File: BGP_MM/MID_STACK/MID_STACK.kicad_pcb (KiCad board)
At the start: 2 copper layers, 20 x 26 mm, 7 parts, among them P1 CONN_01X04, P2 CONN_01X09

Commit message: MM Finished board layouts
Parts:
- added J1: Conn_01x04_Male, Connectors_JST:JST_PH_B4B-PH-K_04x2.00mm_Straight, B.Cu at (152.0, 88.8)
- added J2: Conn_01x02_Male, Connectors_JST:JST_PH_B2B-PH-K_02x2.00mm_Straight, B.Cu at (148.0, 83.6)
- added J3: Conn_01x04_Male, Connectors_JST:JST_PH_B4B-PH-K_04x2.00mm_Straight, B.Cu at (152.0, 99.2)
- added J4: Conn_01x04_Male, Connectors_JST:JST_PH_B4B-PH-K_04x2.00mm_Straight, B.Cu at (152.0, 94.0)
- added P3: CONN_01X02, Terminal_Blocks:TerminalBlock_Pheonix_MPT-2.54mm_2pol, B.Cu at (144.8, 105.6)
- added P4: CONN_01X03, Terminal_Blocks:TerminalBlock_Pheonix_MPT-2.54mm_3pol, B.Cu at (153.1, 105.6)
- C1, C2: footprint Capacitor_THT:C_Rect_L7.2mm_W2.5mm_P5.00mm_FKS2_FKP2_MKS2_MKP2 -> Capacitor_THT:C_Rect_L4.6mm_W3.0mm_P2.50mm_MKS02_FKP02
- P1: value CONN_01X04 -> CONN_01X09; footprint Connectors_JST:JST_PH_B4B-PH-K_04x2.00mm_Straight -> LIBS:Potentiometer_Alpha_Tripple_Vertical_Dual_Shaft
- P2: value CONN_01X09 -> CONN_01X02; footprint LIBS:Potentiometer_Alpha_Tripple_Vertical_Dual_Shaft -> Terminal_Blocks:TerminalBlock_Pheonix_MPT-2.54mm_2pol
- R1: value 4.7k -> 200k
- R2: value 4.7k -> 10k
- R3: value 100k -> 10k
- moved C2 54.3 mm to (130.5, 103.6), turned to 0 degrees
- moved P1 50.1 mm to (132.2, 84.5), turned to 90 degrees
- moved R2 46.5 mm to (137.0, 99.5), turned to 0 degrees
- moved C1 36.5 mm to (130.6, 107.2), turned to 0 degrees
- moved R1 35.6 mm to (132.0, 99.5), turned to 180 degrees
- moved P2 34.2 mm to (139.1, 105.6), turned to 180 degrees
- moved R3 31.5 mm to (142.0, 99.5)
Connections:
- C2 pad 1: /F1_1 -> /MID_R
- P1 pad 1: /MID_I -> Net-(P1-Pad1)
- P1 pad 2: /F1_1 -> /F1_2
- P1 pad 3: /MID_O -> /MID_R
- P1 pad 4: /Vref -> Net-(P1-Pad4)
- P2 pad 1: Net-(P2-Pad1) -> /JZ_I
- P2 pad 2: /F1_2 -> Earth
- R1 pad 2: /F1_2 -> /MID_R
- R2 pad 1: /F2_2 -> Net-(C1-Pad2)
- R2 pad 2: /Vref -> /F1_2
- R3 pad 1: Net-(C1-Pad2) -> /F2_2
- R3 pad 2: /F1_1 -> /Vref
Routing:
- net /MID_R: track 0.00 -> 45.8 mm
- net /F1_1: track 36.3 -> 0.00 mm
- net /JZ_I: track 0.00 -> 18.0 mm
- net /MID_I: track 11.4 -> 26.6 mm
- net /SIG_O: track 0.00 -> 13.0 mm
- net /MM_BH: track 0.00 -> 12.1 mm
- net /MM_NH: track 0.00 -> 7.73 mm
- net /MM_BC: track 0.00 -> 6.63 mm
- net /F2_2: track 15.9 -> 12.0 mm
- net /F1_2: track 14.7 -> 17.5 mm
- net /VOL2: track 16.4 -> 14.9 mm
- net /MID_O: track 12.1 -> 13.3 mm
- net Net-(C1-Pad2): track 12.8 -> 11.7 mm
- added copper zone on B.Cu, net Earth
- removed copper zone on B.Cu, net (none)
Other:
- board size 20 x 26 mm -> 26 x 28 mm

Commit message: MM Tweaks
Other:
- board text added: "MM Sabre Mid Stack CBD Design"
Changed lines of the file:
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@@
     (links 24)
     (no_connects 0)
-    (area 128.924999 80.924999 155.075001 109.075001)
+    (area 127.485 78.666666 155.203001 111.03588)
     (thickness 1.6)
-    (drawings 8)
+    (drawings 9)
     (tracks 64)
     (zones 0)
@@
     )
   )
+  (gr_text "MM Sabre\nMid Stack\nCBD Design" (at 151.8 84) (layer F.SilkS)
+    (effects (font (size 0.6 0.6) (thickness 0.15)))
+  )
   (gr_line (start 129.3 108.7) (end 154.7 108.7) (layer Margin) (width 0.2))

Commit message: MM - Board changes
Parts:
- removed J2: Conn_01x02_Male, Connectors_JST:JST_PH_B2B-PH-K_02x2.00mm_Straight
- removed J3, J4: Conn_01x04_Male, Connectors_JST:JST_PH_B4B-PH-K_04x2.00mm_Straight
- removed P2, P3: CONN_01X02, Terminal_Blocks:TerminalBlock_Pheonix_MPT-2.54mm_2pol
- removed P4: CONN_01X03, Terminal_Blocks:TerminalBlock_Pheonix_MPT-2.54mm_3pol
- C1: footprint Capacitor_THT:C_Rect_L4.6mm_W3.0mm_P2.50mm_MKS02_FKP02 -> Capacitors_SMD:C_0805; moved to F.Cu
- C2: footprint Capacitor_THT:C_Rect_L4.6mm_W3.0mm_P2.50mm_MKS02_FKP02 -> Capacitors_SMD:C_1206; moved to F.Cu
- moved C1 8.98 mm to (137.1, 101.0), turned to 180 degrees
- moved J1 5.90 mm to (146.4, 90.7), turned to 90 degrees
- moved C2 3.00 mm to (132.0, 101.0)
- moved R1 1.50 mm to (132.0, 98.0)
- moved R2 1.50 mm to (137.0, 98.0)
- moved R3 1.50 mm to (142.0, 98.0)
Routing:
- net /JZ_I: track 18.0 -> 0.00 mm
- net /SIG_O: track 13.0 -> 0.00 mm
- net /MM_BH: track 12.1 -> 0.00 mm
- net /MID_R: track 45.8 -> 34.6 mm
- net /MM_NH: track 7.73 -> 0.00 mm
- net /MM_BC: track 6.63 -> 0.00 mm
- net Net-(C1-Pad2): track 11.7 -> 5.88 mm
- net /VOL2: track 14.9 -> 9.70 mm
- net /MID_O: track 13.3 -> 9.83 mm
- net /F1_2: track 17.5 -> 14.4 mm, vias 0 -> 1
- net /MID_I: track 26.6 -> 29.5 mm
- net /Vref: track 0.00 -> 1.00 mm, vias 0 -> 1
- added copper zone on B.Cu, net /Vref
- removed copper zone on B.Cu, net Earth
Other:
- board size 26 x 28 mm -> 19.5 x 21.5 mm

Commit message: tweaks
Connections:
- J1 pad 1: /Vref -> /MID_I
- J1 pad 2: /MID_O -> /MID_R
- J1 pad 3: /MID_R -> /MID_O
- J1 pad 4: /MID_I -> /Vref
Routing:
- net /MID_I: track 29.5 -> 20.1 mm
- net /MID_O: track 9.83 -> 11.3 mm
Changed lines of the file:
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@@
     )
     (pad 1 thru_hole rect (at 0 0 90) (size 1.2 1.7) (drill 0.75) (layers *.Cu *.Mask)
+      (net 4 /MID_I))
+    (pad 2 thru_hole oval (at 2 0 90) (size 1.2 1.7) (drill 0.75) (layers *.Cu *.Mask)
+      (net 10 /MID_R))
+    (pad 3 thru_hole oval (at 4 0 90) (size 1.2 1.7) (drill 0.75) (layers *.Cu *.Mask)
+      (net 5 /MID_O))
+    (pad 4 thru_hole oval (at 6 0 90) (size 1.2 1.7) (drill 0.75) (layers *.Cu *.Mask)
       (net 3 /Vref))
-    (pad 2 thru_hole oval (at 2 0 90) (size 1.2 1.7) (drill 0.75) (layers *.Cu *.Mask)
-      (net 5 /MID_O))
-    (pad 3 thru_hole oval (at 4 0 90) (size 1.2 1.7) (drill 0.75) (layers *.Cu *.Mask)
-      (net 10 /MID_R))
-    (pad 4 thru_hole oval (at 6 0 90) (size 1.2 1.7) (drill 0.75) (layers *.Cu *.Mask)
-      (net 4 /MID_I))
     (model ${KISYS3DMOD}/Connectors_JST.3dshapes/JST_PH_B4B-PH-K_04x2.00mm_Straight.wrl
       (at (xyz 0 0 0))
@@
   (segment (start 133.5 101) (end 134.5 101) (width 0.4) (layer F.Cu) (net 3))
   (via (at 134.5 101) (size 0.6) (drill 0.4) (layers F.Cu B.Cu) (net 3))
-  (segment (start 130.05 84) (end 130.05 92.3) (width 0.4) (layer B.Cu) (net 4))
-  (segment (start 130.05 92.3) (end 132.25 94.5) (width 0.4) (layer B.Cu) (net 4))
-  (segment (start 131.85 82.2) (end 130.05 84) (width 0.4) (layer B.Cu) (net 4))
-  (segment (start 142.7 82.2) (end 131.85 82.2) (width 0.4) (layer B.Cu) (net 4))
-  (segment (start 146.4 84.65) (end 145.15 84.65) (width 0.4) (layer B.Cu) (net 4))
-  (segment (start 145.15 84.65) (end 142.7 82.2) (width 0.4) (layer B.Cu) (net 4))
-  (segment (start 139.75 94.5) (end 139.75 93.2) (width 0.4) (layer B.Cu) (net 5))
-  (segment (start 139.75 93.2) (end 144.3 88.65) (width 0.4) (layer B.Cu) (net 5))
-  (segment (start 144.3 88.65) (end 146.4 88.65) (width 0.4) (layer B.Cu) (net 5))
+  (segment (start 141.45 98) (end 135.75 98) (width 0.4) (layer B.Cu) (net 4))
+  (segment (start 135.75 98) (end 132.25 94.5) (width 0.4) (layer B.Cu) (net 4))
+  (segment (start 146.4 93.05) (end 141.45 98) (width 0.4) (layer B.Cu) (net 4))
+  (segment (start 146.4 90.65) (end 146.4 93.05) (width 0.4) (layer B.Cu) (net 4))
+  (segment (start 146.4 86.65) (end 145.15 86.65) (width 0.4) (layer B.Cu) (net 5))
+  (segment (start 145.15 86.65) (end 142.85 88.95) (width 0.4) (layer B.Cu) (net 5))
+  (segment (start 142.85 88.95) (end 142.85 91.4) (width 0.4) (layer B.Cu) (net 5))
+  (segment (start 142.85 91.4) (end 139.75 94.5) (width 0.4) (layer B.Cu) (net 5))
   (segment (start 138.1 96.9) (end 138.1 86.6) (width 0.4) (layer B.Cu) (net 6))
   (segment (start 138.1 86.6) (end 136 84.5) (width 0.4) (layer B.Cu) (net 6))
@@
   (segment (start 141.7 93.2) (end 139.8 91.3) (width 0.4) (layer F.Cu) (net 7))
   (segment (start 139.8 91.3) (end 137.8 91.3) (width 0.4) (layer F.Cu) (net 7))
-  (segment (start 139.75 84.5) (end 139.75 86.65) (width 0.4) (layer B.Cu) (net 10))
-  (segment (start 139.75 86.65) (end 139.75 89.5) (width 0.4) (layer B.Cu) (net 10))
-  (segment (start 146.4 86.65) (end 145.15 86.65) (width 0.4) (layer B.Cu) (net 10))
-  (segment (start 145.15 86.65) (end 139.75 86.65) (width 0.4) (layer B.Cu) (net 10))
+  (segment (start 141.45 87.8) (end 139.7 87.8) (width 0.4) (layer F.Cu) (net 10))
+  (segment (start 146.4 88.65) (end 144.7 88.65) (width 0.4) (layer F.Cu) (net 10))
+  (segment (start 144.7 88.65) (end 143.85 87.8) (width 0.4) (layer F.Cu) (net 10))
+  (segment (start 143.85 87.8) (end 141.45 87.8) (width 0.4) (layer F.Cu) (net 10))
+  (segment (start 139.75 84.5) (end 139.75 87.75) (width 0.4) (layer F.Cu) (net 10))
+  (segment (start 139.75 87.75) (end 139.75 89.5) (width 0.4) (layer F.Cu) (net 10))
+  (segment (start 130.9 98) (end 130.9 97.15) (width 0.4) (layer F.Cu) (net 10))
+  (segment (start 130.9 97.15) (end 130.4 96.65) (width 0.4) (layer F.Cu) (net 10))
+  (segment (start 130.4 96.65) (end 130.4 89) (width 0.4) (layer F.Cu) (net 10))
+  (segment (start 131.6 87.8) (end 139.7 87.8) (width 0.4) (layer F.Cu) (net 10))
+  (segment (start 130.4 89) (end 131.6 87.8) (width 0.4) (layer F.Cu) (net 10))
+  (segment (start 139.7 87.8) (end 139.75 87.75) (width 0.4) (layer F.Cu) (net 10))
   (segment (start 130.5 99.6) (end 130.9 99.2) (width 0.4) (layer F.Cu) (net 10))
   (segment (start 130.9 99.2) (end 130.9 98) (width 0.4) (layer F.Cu) (net 10))
   (segment (start 130.5 101) (end 130.5 99.6) (width 0.4) (layer F.Cu) (net 10))
-  (segment (start 130.9 98) (end 130.9 97.15) (width 0.4) (layer F.Cu) (net 10))
-  (segment (start 130.4 89) (end 131.6 87.8) (width 0.4) (layer F.Cu) (net 10))
-  (segment (start 130.9 97.15) (end 130.4 96.65) (width 0.4) (layer F.Cu) (net 10))
-  (segment (start 130.4 96.65) (end 130.4 89) (width 0.4) (layer F.Cu) (net 10))
-  (segment (start 131.6 87.8) (end 138.05 87.8) (width 0.4) (layer F.Cu) (net 10))
-  (segment (start 138.05 87.8) (end 138.850001 88.600001) (width 0.4) (layer F.Cu) (net 10))
-  (segment (start 138.850001 88.600001) (end 139.75 89.5) (width 0.4) (layer F.Cu) (net 10))
   (zone (net 3) (net_name /Vref) (layer F.Cu) (hatch edge 0.508)
     (connect_pads (clearance 0.3))

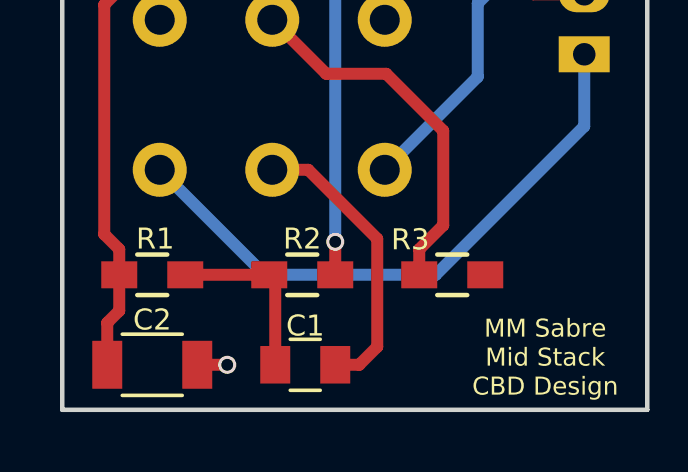
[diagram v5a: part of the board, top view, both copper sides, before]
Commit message: MM Gerbers Finished, Mid Stack Ammended J0
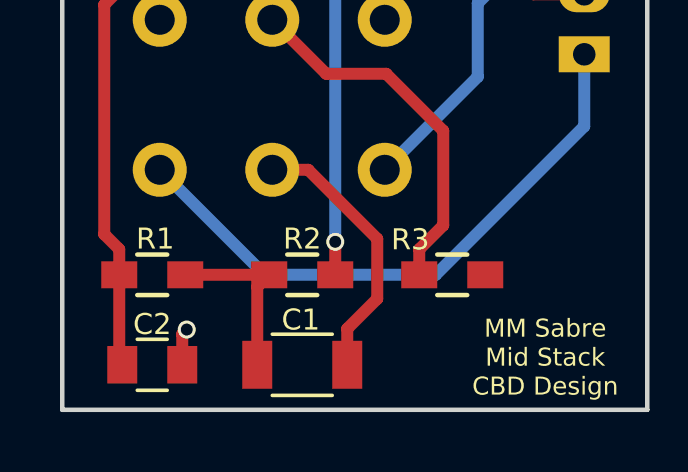
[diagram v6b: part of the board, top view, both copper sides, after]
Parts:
- C1: footprint Capacitors_SMD:C_0805 -> Capacitors_SMD:C_1206
- C2: footprint Capacitors_SMD:C_1206 -> Capacitors_SMD:C_0805
- moved C1 0.10 mm to (137.0, 101.0)
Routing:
- net /VOL2: track 9.70 -> 9.07 mm
